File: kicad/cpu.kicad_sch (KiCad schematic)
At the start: 11 parts, among them IC1 Z180, U24 GAL16V8, U31 GAL16V8, Y2 12.288 MHz

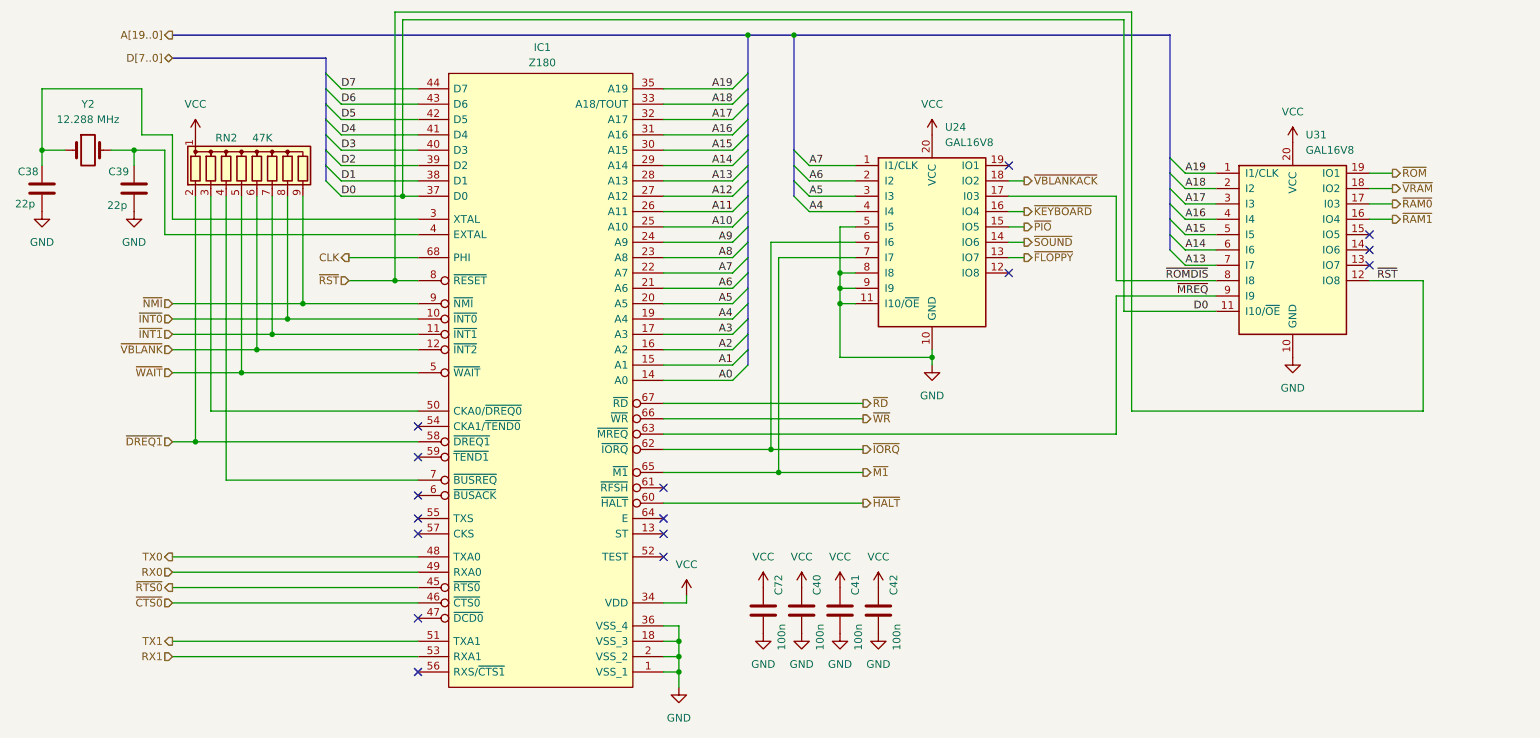
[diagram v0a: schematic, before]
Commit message: hw: adapt to the changes in memory decoder pinout
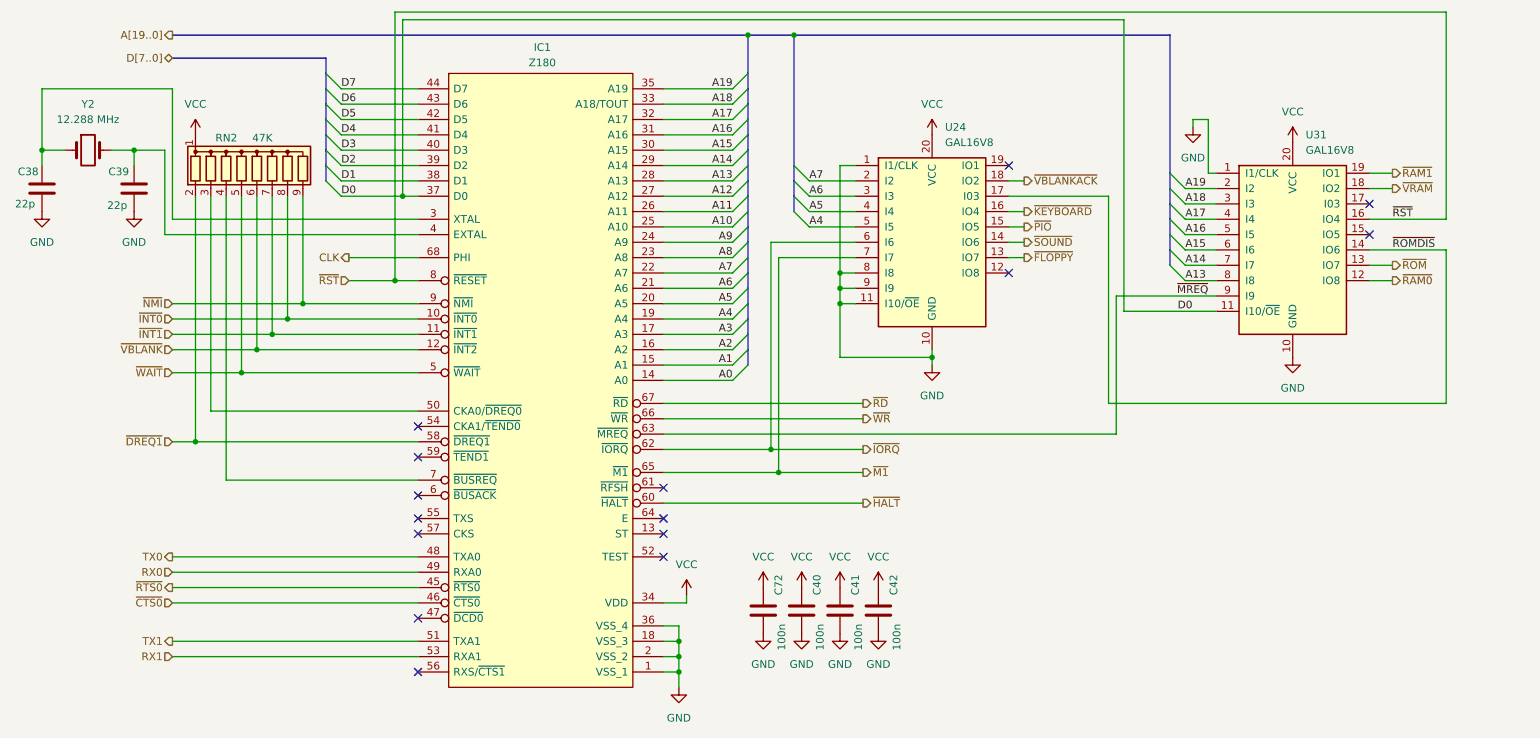
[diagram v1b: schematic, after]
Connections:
- net A13: now also U31.8 (I8); no longer U31.7 (I7)
- net A14: now also U31.7 (I7); no longer U31.6 (I6)
- net A15: now also U31.6 (I6); no longer U31.5 (I5)
- net A16: now also U31.5 (I5); no longer U31.4 (I4)
- net A17: now also U31.4 (I4); no longer U31.3 (I3)
- net A18: now also U31.3 (I3); no longer U31.2 (I2)
- net A19: now also U31.2 (I2); no longer U31.1 (I1/CLK)
- net A4: now also U24.5 (I5); no longer U24.4 (I4)
- net A5: now also U24.4 (I4); no longer U24.3 (I3)
- net A6: now also U24.3 (I3); no longer U24.2 (I2)
- net A7: now also U24.2 (I2); no longer U24.1 (I1/CLK)
- net GND: now also U24.1 (I1/CLK), U31.1 (I1/CLK); no longer U24.5 (I5)
- net ~{RAM0}: now also U31.12 (IO8); no longer U31.17 (I03)
- net ~{RAM1}: now also U31.19 (IO1); no longer U31.16 (IO4)
- net ~{ROMDIS}: now also U31.14 (IO6); no longer U31.8 (I8)
- net ~{ROM}: now also U31.13 (IO7); no longer U31.19 (IO1)
- net ~{RST}: now also U31.16 (IO4); no longer U31.12 (IO8)
- no-connect marks 16 -> 15

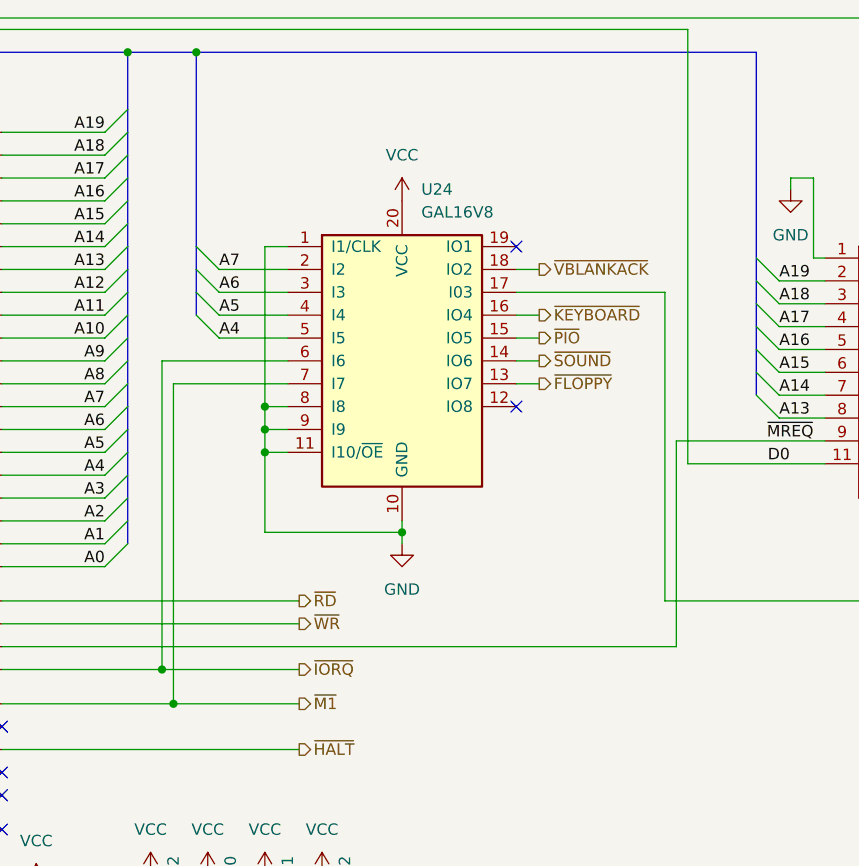
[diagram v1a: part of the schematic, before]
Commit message: hw: color text mode VGA (WIP)
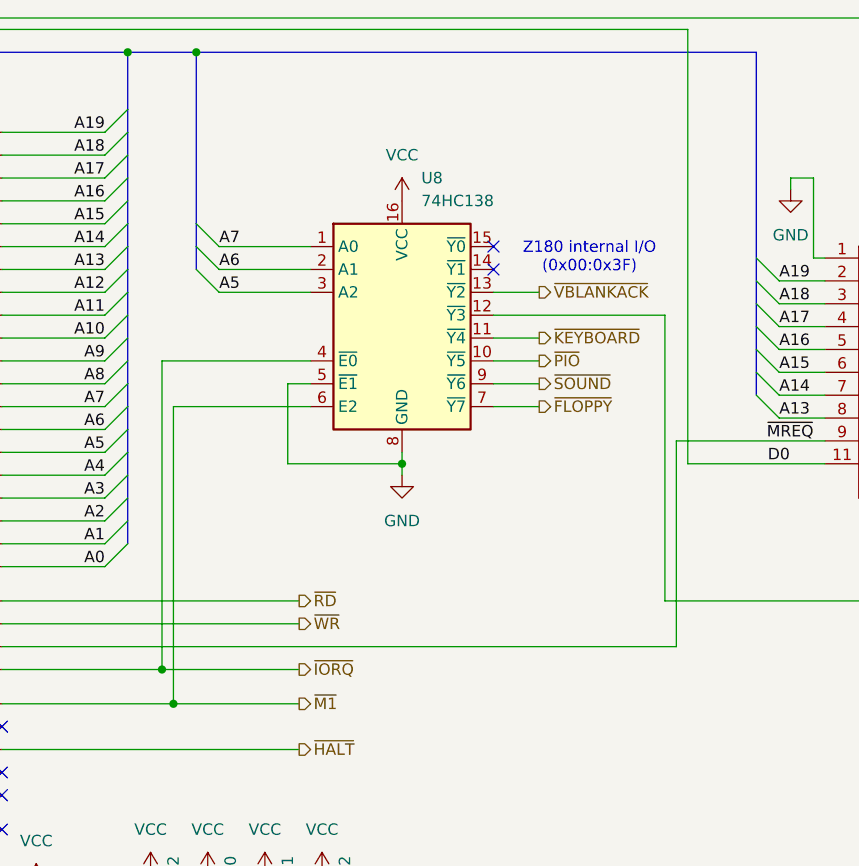
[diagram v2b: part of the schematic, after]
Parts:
- removed U24: GAL16V8, Package_DIP:DIP-20_W7.62mm, symbol Logic_Programmable:GAL16V8
- added U8: 74HC138, Package_DIP:DIP-16_W7.62mm, symbol 74xx:74HC138
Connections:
- net A5: now also U8.3 (A2)
- net A6: now also U8.2 (A1)
- net A7: now also U8.1 (A0)
- net GND: now also U8.5 (~{E1}), U8.8 (GND)
- net VCC: now also U8.16 (VCC)
- net ~{FLOPPY}: now also U8.7 (~{Y7})
- net ~{IORQ}: now also U8.4 (~{E0})
- net ~{KEYBOARD}: now also U8.11 (~{Y4})
- net ~{M1}: now also U8.6 (E2)
- net ~{PIO}: now also U8.10 (~{Y5})
- net ~{ROMDIS}: now also U8.12 (~{Y3})
- net ~{SOUND}: now also U8.9 (~{Y6})
- net ~{VBLANKACK}: now also U8.13 (~{Y2})
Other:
- note added: "Z180 internal I/O (0x00:0x3F)"

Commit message: hw: finish schematic, start routing
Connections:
- net ~{FLOPPY} renamed ~{CF}
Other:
- company: (none) -> A.K.
- title: (none) -> Z180 CPU
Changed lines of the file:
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@@
 	(generator_version "9.0")
 	(paper "A4")
+	(title_block
+		(title "Z180 CPU")
+		(date "2025-06-18")
+		(rev "A")
+		(company "A.K.")
+	)
 	(text "Z180 internal I/O\n(0x00:0x3F)"
 		(exclude_from_sim no)
@@
 				(size 1.27 1.27)
 			)
+		)
+	)
+	(text_box "GAL16V8\nZAK181MD\n\nNC A19 A18 A17 A16 A15 A14 A13 /MREQ GND\nDAT /RAM0 /ROM /ROMCTRL NC /RST ROMDIS /VRAM /RAM1 VCC\n\nVRAM = A13 * A14 * A15 * A16 * A17 * A18 * A19 * MREQ\nROM = /A14 * /A15 * /A16 * /A17 * /A18 * /A19 * MREQ * /ROMDIS\nRAM0 = /VRAM * /ROM * MREQ * /A19\nRAM1 = /VRAM * /ROM * MREQ * A19\n\nROMDIS = /RST * ROMCTRL * DAT + /RST * /ROMCTRL * ROMDIS\n\nDESCRIPTION\n\nZAK181 SBC Memory decoder\n"
+		(exclude_from_sim no)
+		(at 199.39 115.57 0)
+		(size 73.66 34.29)
+		(margins 0.9525 0.9525 0.9525 0.9525)
+		(stroke
+			(width 0)
+			(type solid)
+		)
+		(fill
+			(type none)
+		)
+		(effects
+			(font
+				(size 1.27 1.27)
+			)
+			(justify left top)
 		)
 	)
@@
 		)
 	)
-	(hierarchical_label "~{FLOPPY}"
+	(hierarchical_label "~{CF}"
 		(shape output)
 		(at 196.85 80.01 0)
